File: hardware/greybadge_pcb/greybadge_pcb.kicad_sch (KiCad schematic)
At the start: 97 parts, among them J1 Conn_02x05_Row_Letter_First, J2 Conn_02x05_Row_Letter_First, J3 Conn_02x05_Row_Letter_First, J4 Conn_02x05_Row_Letter_First, J5 78171-0002, Q1 2N7002, SW1 SW_SPST, SW2 SW_Push, SW3 SW_Push, SW4 SW_Push, SW5 SW_Push, SW6 SW_Push, SW7 SW_Push, SW8 SW_Push, U1 GC9A01_IPS_display, U2 BQ24075, U3 TLV62568DBV, U4 TLV62568DBV, U5 TLV73325PDBV

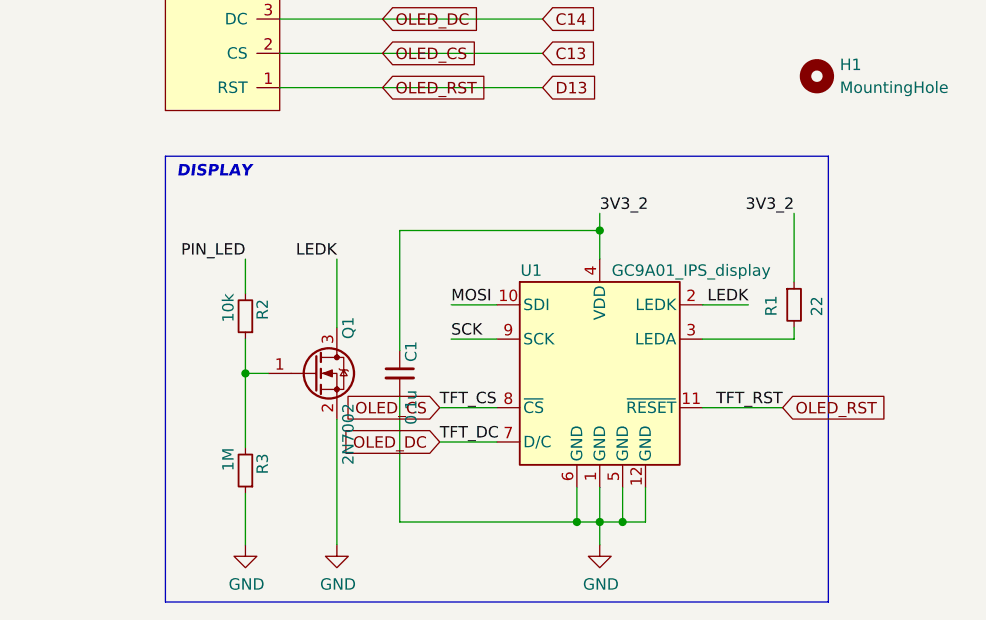
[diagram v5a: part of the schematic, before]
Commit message: Update to on-board OLED
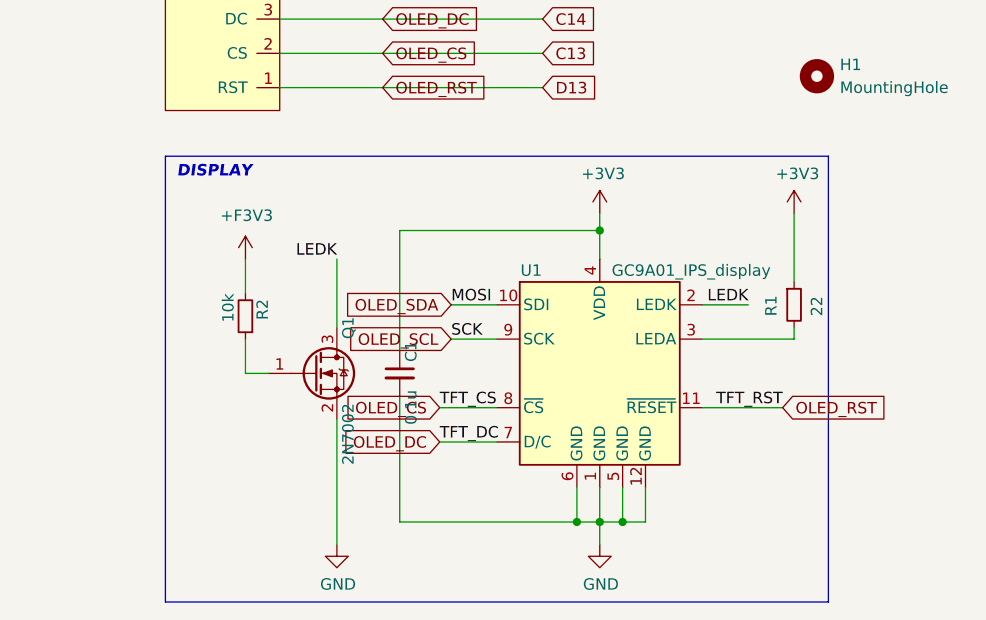
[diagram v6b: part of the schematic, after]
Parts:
- removed R3: 1M, Resistor_SMD:R_0603_1608Metric, symbol Device:R_Small
- C1: footprint Capacitor_SMD:C_0603_1608Metric -> Capacitor_SMD:C_0402_1005Metric
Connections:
- net 3V3_2 is gone; now on net +3V3: C1.1, R1.1, U1.4 (VDD)
- net MOSI is gone; now on net D14: U1.10 (SDI)
- net PIN_LED is gone; now on net +F3V3: R2.2
- net SCK is gone; now on net E14: U1.9 (SCK)
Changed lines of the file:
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@@
 	)
 	(junction
-		(at 212.09 311.15)
-		(diameter 0)
-		(color 0 0 0 0)
-	)
-	(junction
 		(at 97.79 212.09)
 		(diameter 0)
@@
 	(wire
 		(pts
-			(xy 212.09 330.2) (xy 212.09 324.485)
-		)
-		(stroke
-			(width 0)
-			(type default)
-		)
-	)
-	(wire
-		(pts
 			(xy 307.34 124.46) (xy 307.34 156.21)
 		)
@@
 	(wire
 		(pts
-			(xy 212.09 311.15) (xy 212.09 319.405)
-		)
-		(stroke
-			(width 0)
-			(type default)
-		)
-	)
-	(wire
-		(pts
 			(xy 212.09 311.15) (xy 214.63 311.15)
 		)
@@
 		)
 	)
-	(label "3V3_2"
-		(at 251.46 293.37 0)
-		(effects
-			(font
-				(size 1.27 1.27)
-			)
-			(justify left bottom)
-		)
-	)
-	(label "PIN_LED"
-		(at 212.09 298.45 180)
-		(effects
-			(font
-				(size 1.27 1.27)
-			)
-			(justify right bottom)
-		)
-	)
-	(label "3V3_2"
-		(at 273.05 293.37 180)
-		(effects
-			(font
-				(size 1.27 1.27)
-			)
-			(justify right bottom)
-		)
-	)
 	(label "TMR"
 		(at 325.12 138.43 0)
@@
 		)
 	)
+	(global_label "OLED_SCL"
+		(shape input)
+		(at 234.95 307.34 180)
+		(fields_autoplaced yes)
+		(effects
+			(font
+				(size 1.27 1.27)
+			)
+			(justify right)
+		)
+		(property "Intersheetrefs" "${INTERSHEET_REFS}"
+			(at 222.712 307.34 0)
+			(effects
+				(font
+					(size 1.27 1.27)
+				)
+				(justify right)
+				(hide yes)
+			)
+		)
+	)
 	(global_label "B12"
 		(shape input)
@@
 		)
 	)
+	(global_label "OLED_SDA"
+		(shape input)
+		(at 234.95 303.53 180)
+		(fields_autoplaced yes)
+		(effects
+			(font
+				(size 1.27 1.27)
+			)
+			(justify right)
+		)
+		(property "Intersheetrefs" "${INTERSHEET_REFS}"
+			(at 222.6515 303.53 0)
+			(effects
+				(font
+					(size 1.27 1.27)
+				)
+				(justify right)
+				(hide yes)
+			)
+		)
+	)
 	(global_label "OLED_CS"
 		(shape input)
@@
 	)
 	(symbol
+		(lib_id "power:+3V3")
+		(at 273.05 293.37 0)
+		(unit 1)
+		(exclude_from_sim no)
+		(in_bom yes)
+		(on_board yes)
+		(dnp no)
+		(property "Reference" "#PWR0129"
+			(at 273.05 297.18 0)
+			(effects
+				(font
+					(size 1.27 1.27)
+				)
+				(hide yes)
+			)
+		)
+		(property "Value" "+3V3"
+			(at 273.431 288.9758 0)
+			(effects
+				(font
+					(size 1.27 1.27)
+				)
+			)
+		)
+		(property "Footprint" ""
+			(at 273.05 293.37 0)
+			(effects
+				(font
+					(size 1.27 1.27)
+				)
+				(hide yes)
+			)
+		)
+		(property "Datasheet" ""
+			(at 273.05 293.37 0)
+			(effects
+				(font
+					(size 1.27 1.27)
+				)
+				(hide yes)
+			)
+		)
+		(property "Description" ""
+			(at 273.05 293.37 0)
+			(effects
+				(font
+					(size 1.27 1.27)
+				)
+			)
+		)
+		(pin "1"
+		)
+		(instances
+			(project "greybadge_pcb"
+				(path "/4eb7ff30-5b75-4e83-8e37-4e6cd7a9e830"
+					(reference "#PWR0129")
+					(unit 1)
+				)
+			)
+		)
+	)
+	(symbol
 		(lib_id "power:+2V5")
 		(at 29.21 261.62 0)
@@
 	(symbol
 		(lib_id "power:+3.3V")
+		(at 212.09 298.45 0)
+		(unit 1)
+		(exclude_from_sim no)
+		(in_bom yes)
+		(on_board yes)
+		(dnp no)
+		(property "Reference" "#PWR0127"
+			(at 212.09 302.26 0)
+			(effects
+				(font
+					(size 1.27 1.27)
+				)
+				(hide yes)
+			)
+		)
+		(property "Value" "+F3V3"
+			(at 209.296 293.624 0)
+			(effects
+				(font
+					(size 1.27 1.27)
+				)
+				(justify left)
+			)
+		)
+		(property "Footprint" ""
+			(at 212.09 298.45 0)
+			(effects
+				(font
+					(size 1.27 1.27)
+				)
+				(hide yes)
+			)
+		)
+		(property "Datasheet" ""
+			(at 212.09 298.45 0)
+			(effects
+				(font
+					(size 1.27 1.27)
+				)
+				(hide yes)
+			)
+		)
+		(property "Description" ""
+			(at 212.09 298.45 0)
+			(effects
+				(font
+					(size 1.27 1.27)
+				)
+			)
+		)
+		(pin "1"
+		)
+		(instances
+			(project "greybadge_pcb"
+				(path "/4eb7ff30-5b75-4e83-8e37-4e6cd7a9e830"
+					(reference "#PWR0127")
+					(unit 1)
+				)
+			)
+		)
+	)
+	(symbol
+		(lib_id "power:+3.3V")
 		(at 33.02 123.19 0)
 		(mirror y)
@@
 	)
 	(symbol
-		(lib_id "Device:R_Small")
-		(at 212.09 321.945 180)
-		(unit 1)
-		(exclude_from_sim no)
-		(in_bom yes)
-		(on_board yes)
-		(dnp no)
-		(property "Reference" "R3"
-			(at 213.995 320.04 90)
-			(effects
-				(font
-					(size 1.27 1.27)
-				)
-				(justify left)
-			)
-		)
-		(property "Value" "1M"
-			(at 210.185 319.405 90)
-			(effects
-				(font
-					(size 1.27 1.27)
-				)
-				(justify left)
-			)
-		)
-		(property "Footprint" "Resistor_SMD:R_0603_1608Metric"
-			(at 212.09 321.945 0)
-			(effects
-				(font
-					(size 1.27 1.27)
-				)
-				(hide yes)
-			)
-		)
-		(property "Datasheet" "~"
-			(at 212.09 321.945 0)
-			(effects
-				(font
-					(size 1.27 1.27)
-				)
-				(hide yes)
-			)
-		)
-		(property "Description" ""
-			(at 212.09 321.945 0)
-			(effects
-				(font
-					(size 1.27 1.27)
-				)
-			)
-		)
-		(pin "1"
-		)
-		(pin "2"
-		)
-		(instances
-			(project "greybadge_pcb"
-				(path "/4eb7ff30-5b75-4e83-8e37-4e6cd7a9e830"
-					(reference "R3")
-					(unit 1)
-				)
-			)
-		)
-	)
-	(symbol
 		(lib_id "power:GND")
 		(at 144.78 57.15 0)
@@
 	)
 	(symbol
+		(lib_id "power:+3V3")
+		(at 251.46 293.37 0)
+		(unit 1)
+		(exclude_from_sim no)
+		(in_bom yes)
+		(on_board yes)
+		(dnp no)
+		(property "Reference" "#PWR0128"
+			(at 251.46 297.18 0)
+			(effects
+				(font
+					(size 1.27 1.27)
+				)
+				(hide yes)
+			)
+		)
+		(property "Value" "+3V3"
+			(at 251.841 288.9758 0)
+			(effects
+				(font
+					(size 1.27 1.27)
+				)
+			)
+		)
+		(property "Footprint" ""
+			(at 251.46 293.37 0)
+			(effects
+				(font
+					(size 1.27 1.27)
+				)
+				(hide yes)
+			)
+		)
+		(property "Datasheet" ""
+			(at 251.46 293.37 0)
+			(effects
+				(font
+					(size 1.27 1.27)
+				)
+				(hide yes)
+			)
+		)
+		(property "Description" ""
+			(at 251.46 293.37 0)
+			(effects
+				(font
+					(size 1.27 1.27)
+				)
+			)
+		)
+		(pin "1"
+		)
+		(instances
+			(project "greybadge_pcb"
+				(path "/4eb7ff30-5b75-4e83-8e37-4e6cd7a9e830"
+					(reference "#PWR0128")
+					(unit 1)
+				)
+			)
+		)
+	)
+	(symbol
 		(lib_id "Device:C")
 		(at 97.79 186.69 0)
@@
 			)
 		)
-		(property "Footprint" "Capacitor_SMD:C_0603_1608Metric"
+		(property "Footprint" "Capacitor_SMD:C_0402_1005Metric"
 			(at 229.235 311.15 0)
 			(effects
@@
 					(unit 1)
 				)
-			)
-		)
-	)
-	(symbol
-		(lib_id "power:GND")
-		(at 212.09 330.2 0)
-		(unit 1)
-		(exclude_from_sim no)
-		(in_bom yes)
-		(on_board yes)
-		(dnp no)
-		(property "Reference" "#PWR015"
-			(at 212.09 336.55 0)
-			(effects
-				(font
-					(size 1.27 1.27)
-				)
-				(hide yes)
-			)
-		)
-		(property "Value" "GND"
-			(at 212.217 334.5942 0)
-			(effects
-				(font
-					(size 1.27 1.27)
-				)
-			)
-		)
-		(property "Footprint" ""
-			(at 212.09 330.2 0)
-			(effects
-				(font
-					(size 1.27 1.27)
-				)
-				(hide yes)
-			)
-		)
-		(property "Datasheet" ""
-			(at 212.09 330.2 0)
-			(effects
-				(font
-					(size 1.27 1.27)
-				)
-				(hide yes)
-			)
-		)
-		(property "Description" ""
-			(at 212.09 330.2 0)
-			(effects
-				(font
-					(size 1.27 1.27)
-				)
-			)
-		)
-		(pin "1"
-		)
-		(instances
-			(project "greybadge_pcb"
-				(path "/4eb7ff30-5b75-4e83-8e37-4e6cd7a9e830"
-					(reference "#PWR015")
-					(unit 1)
-				)

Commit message: feat: oled + jtag
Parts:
- removed J1: Conn_02x05_Row_Letter_First, Connector_PinSocket_2.54mm:PinSocket_2x06_P2.54mm_Horizontal, symbol Connector_Generic:Conn_02x06_Odd_Even
- added JP4, JP5, JP6, JP7, JP8: SolderJumper_2_Bridged, Jumper:SolderJumper-2_P1.3mm_Bridged2Bar_RoundedPad1.0x1.5mm, symbol Jumper:SolderJumper_2_Bridged
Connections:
- net C13: now also GC9A1.4 (SDA), U1.10 (SDI); no longer GC9A1.2 (CS), U1.8 (~{CS})
- net C14: now also GC9A1.5 (SCL), U1.9 (SCK); no longer GC9A1.3 (DC), U1.7 (D/C)
- net D14: now also GC9A1.2 (CS), U1.8 (~{CS}); no longer GC9A1.4 (SDA), U1.10 (SDI)
- net E14: now also GC9A1.3 (DC), U1.7 (D/C); no longer GC9A1.5 (SCL), U1.9 (SCK)
- net GPIO16: now also JP4.2 (B)
- net GPIO17: now also JP5.2 (B)
- net GPIO18: now also JP6.2 (B)
- net GPIO19: now also JP7.2 (B)
- net GPIO20: now also JP8.2 (B)
- net creset: now also JP8.1 (A)
- net fpga_tck: now also JP7.1 (A)
- net fpga_tdi: now also JP6.1 (A)
- net fpga_tdo: now also JP4.1 (A)
- net fpga_tms: now also JP5.1 (A)
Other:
- moved on the sheet: AA+1, AA-1, C2, C3, C4, C5, C6, C7, C8, C9, D1, J5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

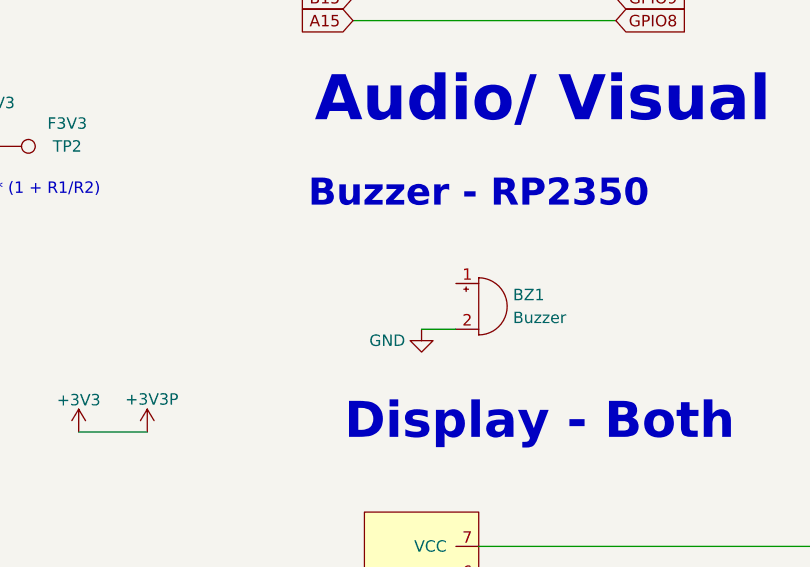
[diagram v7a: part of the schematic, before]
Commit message: Route buzzer, improve routing/silkscreen ref
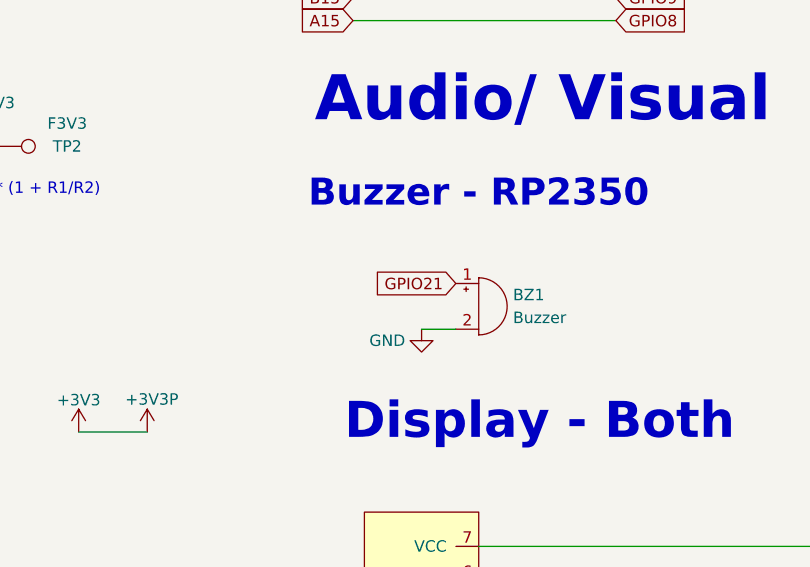
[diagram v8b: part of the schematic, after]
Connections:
- net GPIO21: now reaches BZ1.1 (+)
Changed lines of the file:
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@@
 			"agBpADEAWgBmAHkAbwAwAHIAcABVADMAQQBBAEYAUgBuAEwAagBhAHUAVgAzAHQARgAwACsAZAAz"
 			"AEYATAByAFoAMQBIAHYAYgBiAFYAegArAHUAUQB6AFYAcgBSADAAVABHAGwAdgA3ADIAUwB2AGYA"
-			"bgBoAHcAOQA1AHMAYgAxAG0AOQA0AHgATgBwAGgAbAB4ADAAMgA2AHEAeQB3AEsAcwBLAA=="
+			"bgBoAHcAOQA1AHMAYgAxAG0AOQA0AHgATgBwAGgAbAB4ADAAMgA2AHEAeQB3AEsAcwBLAE4ASwBn"
+			"AFQASAA3AE4AVgA2AGIAdQAyAFoAZABNADcAYwBzAHkAKwB3ADUAZgBFAGUASgBkAEUASQBnAEsA"
+			"cABIAGMAeQBWAHoAeABQAE4AWQA2AEMAMgBoAEQAQwBWAFIATQBOAE8AKwB2AFgAdgB2AHUAZQA4"
+			"AEgAdwAwAFAAMQA3AHUANwB1AHkAeQA2ACsAWgBNAEsARQBDAFYANwBFAEUARwBkADUAeABtAHcA"
+			"TwBIAGoAeQAwAFoAYwB1AFcAYQByAFcANgBhAE0ARQBDAE4ARgB3AG4AUgB2AHQASgBxAFMAaABF"
+			"AFYAVQBpAGIAMQBhAGQAaABTADgASQBaAHgARABNAEcAVwAwAHIAagB6ADcAKwB3AFoAKwBFADUA"
+			"SwBNAGUANgBhAGMAdgBhAGUAeAArADIAUQAzAFcAUQBPAC8AdQBDADUAYQBqAEUATAB6ADMANgBL"
+			"AE4AVwBHAFcAOABSAFkAQQB3ACsAdABWADAAdABuAHIARgBpAEMAbAB0AFkAWABIAG4AdwBBAGIA"
+			"TwAyADQAOQBnAFgAdgB1AHcANQBUAHAAcQBEAC8AOABHAHQAUABQAE4AbgAvADQAcQB0AGQAawBy"
+			"AEgARgBZAGMAMwA3AE8AdABzAFgAZgBlAHEAVAArAE8AYQBkAGcANgA5AHUAVABvAFkARwB1AEsA"
+			"VgAxAEQAOQBHADQATQAyAGYAUABQAC8AOAA4AE0AMwBHAEMANwBPADkANwA3AGEAbABuACsAdABh"
+			"AC8AMQBPAEYAYwA3AEwAaAB1ADcAWgBTAEwAVgB5AFoASgBzAHUAWAArACsAOABwAHMAVgBMAFIA"
+			"dQAwAE0ALwBSADQAdQB0AHYAMABEAGUAMgBQAGYAUAB5AHUAdgBOAHUAdQBnAG0AdAByAFkAUABE"
+			"ADkAUwBSAEoAaAByAE4AQgBFADEAbQBBAHEAMABLAGMAMQBSACsALwArAC8AdQBEAGYAMwBmAEgA"
+			"awBzAC8AOQBuADYAYwA5ACsAOQB6AHUAOQBhACsAMABpAE0AUQBpAHgAWQBHAFAAWQBRAHgAagBl"
+			"AEwAdgB4AGwAbQBxAG0AUwBJAGoASgBBAHQAYQBUAEYAVQBiAEQAbQBpAEQATQBVADgAYwBKADEA"
+			"RgBpAGgAUQBNAFkANQBnAG8ARwBWAHEAawBXAFUASgBFAG4AMgBGAGcAegA0AGcANABTAHcAcQBI"
+			"ADkAWABrAHUAQwBCAFIAYQBwAFEAZwBwAHIASQBHAEMAZwBEAG8AdQBxAEQAZgBUAHIAQgBxAEYA"
+			"bwBBAEIARgBGADEAUgBBAHcATwBZADYAVgBSAFYAVgBFAEIASwBRAGkAawBIAGcAUQBQAA=="
 		)
 	)
@@
 				(hide yes)
 			)
+		)
+	)
+	(global_label "GPIO21"
+		(shape input)
+		(at 213.36 227.33 180)
+		(fields_autoplaced yes)
+		(effects
+			(font
+				(size 1.27 1.27)
+			)
+			(justify right)
+		)
+		(property "Intersheetrefs" "${INTERSHEET_REFS}"
+			(at 203.4805 227.33 0)
+			(effects
+				(font
+					(size 1.27 1.27)
+				)
+				(justify right)
+				(hide yes)
+			)
